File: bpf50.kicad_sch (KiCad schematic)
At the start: 39 parts

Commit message: 部品定数を入力　ただし未評価
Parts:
- C201, C230: value 10p -> NM
- C202, C229: value 10p -> 1000p
- C203, C205, C207, C209, C211, C213, C215, C217, C219, C221, C223, C225, C227: value 1p -> NM
- C204, C206, C210, C220, C226, C228: value 10p -> 150p
- C214, C218: value 10p -> 68p
- L203, L205: value 10n -> NM
- L204, L206: value 1u -> 33n
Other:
- note added: "2t D8.0mm L4.0mm"
- note added: "Butterworth 45M-57M 72p, 36p, 149p"
- company: (none) -> JK1MLY / PRUG
- title: (none) -> FM QRP TRCV

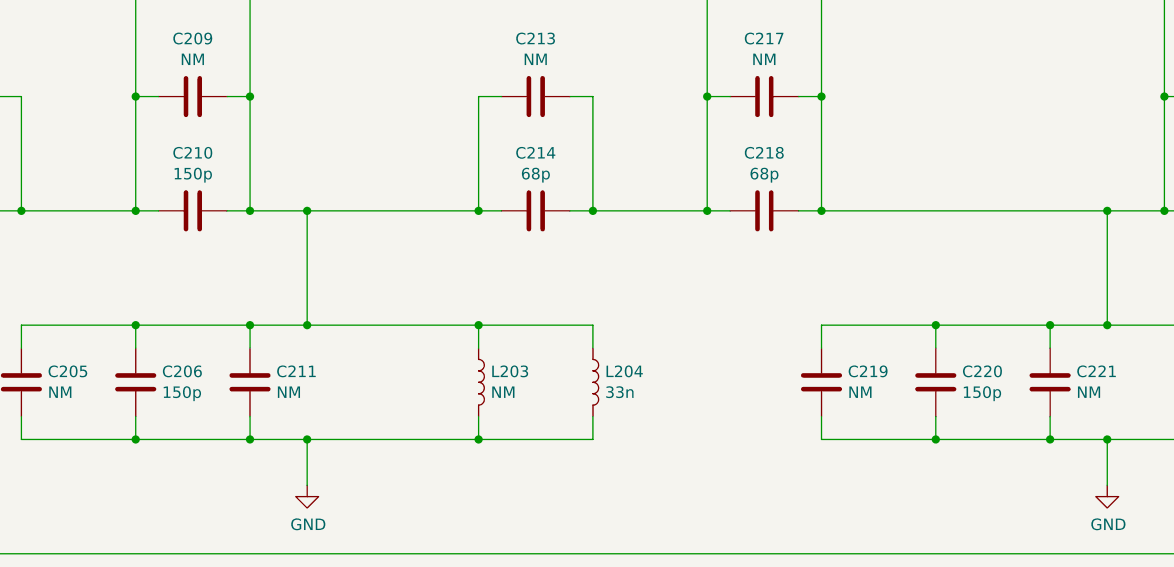
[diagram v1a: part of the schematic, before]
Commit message: バンドパスフィルタの定数を見直し（単体試験の反映）
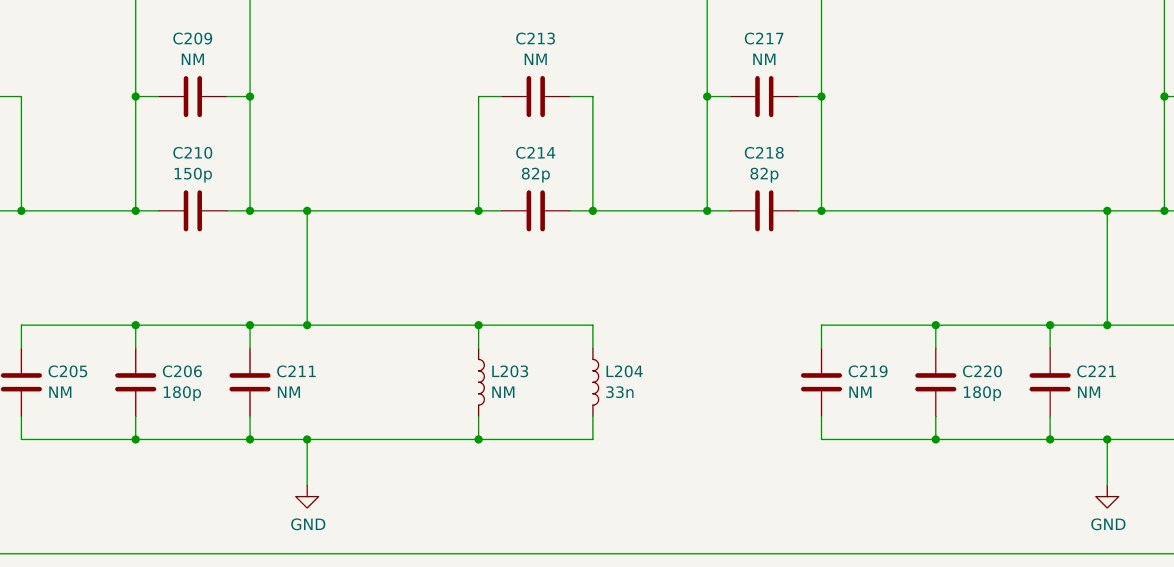
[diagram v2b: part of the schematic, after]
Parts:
- C206, C220: value 150p -> 180p
- C214, C218: value 68p -> 82p
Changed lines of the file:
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@@
       (effects (font (size 1.27 1.27)) (justify left))
     )
-    (property "Value" "150p" (id 1) (at 180.721 96.393 0)
+    (property "Value" "180p" (id 1) (at 180.721 96.393 0)
       (effects (font (size 1.27 1.27)) (justify left))
     )
@@
     (in_bom yes) (on_board yes)
     (property "Reference" "C218" (id 0) (at 158.75 69.7992 90))
-    (property "Value" "68p" (id 1) (at 158.75 72.1106 90))
+    (property "Value" "82p" (id 1) (at 158.75 72.1106 90))
     (property "Footprint" "Capacitor_THT:C_Disc_D3.4mm_W2.1mm_P2.50mm" (id 2) (at 162.56 75.2348 0)
       (effects (font (size 1.27 1.27)) hide)
@@
     (in_bom yes) (on_board yes)
     (property "Reference" "C214" (id 0) (at 133.35 69.7992 90))
-    (property "Value" "68p" (id 1) (at 133.35 72.1106 90))
+    (property "Value" "82p" (id 1) (at 133.35 72.1106 90))
     (property "Footprint" "Capacitor_THT:C_Disc_D3.4mm_W2.1mm_P2.50mm" (id 2) (at 137.16 75.2348 0)
       (effects (font (size 1.27 1.27)) hide)
@@
       (effects (font (size 1.27 1.27)) (justify left))
     )
-    (property "Value" "150p" (id 1) (at 91.821 96.393 0)
+    (property "Value" "180p" (id 1) (at 91.821 96.393 0)
       (effects (font (size 1.27 1.27)) (justify left))
     )

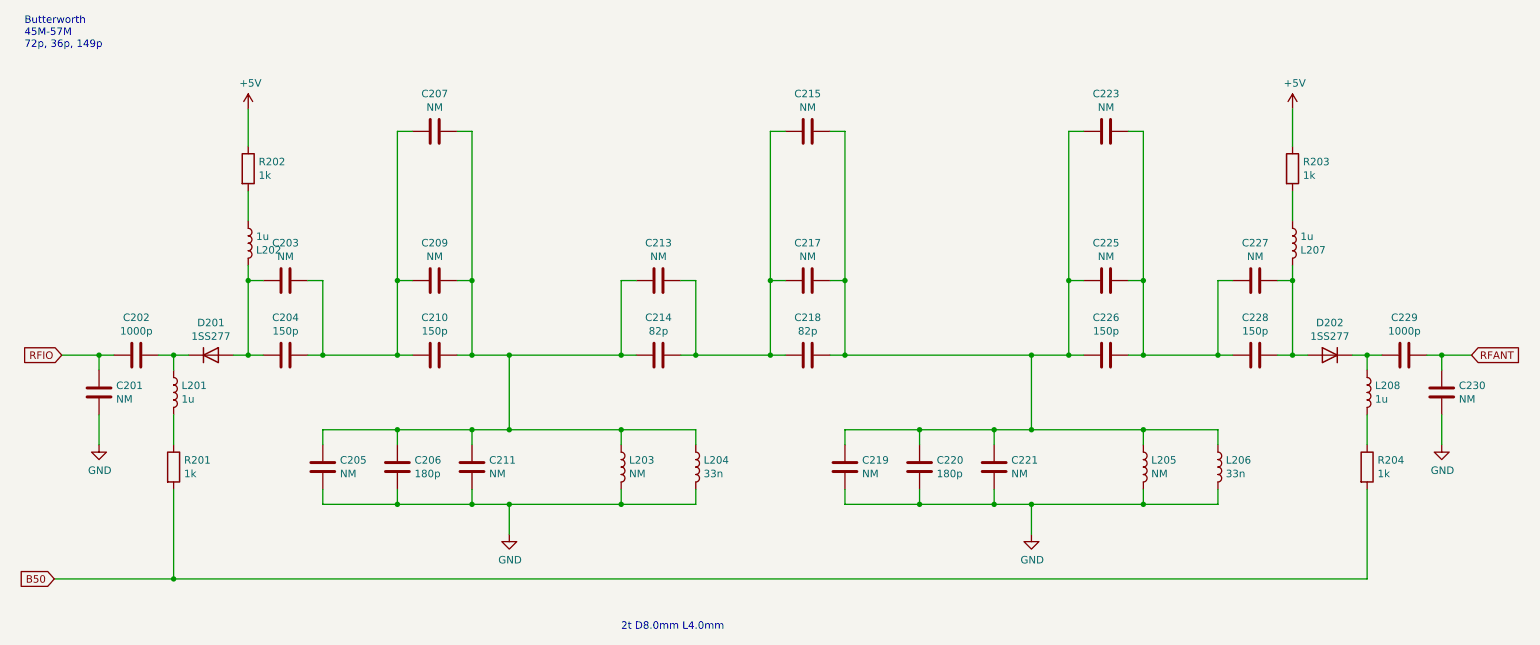
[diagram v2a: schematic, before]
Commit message: Add files via upload
フィルタ回路変更とジャンパクリーン
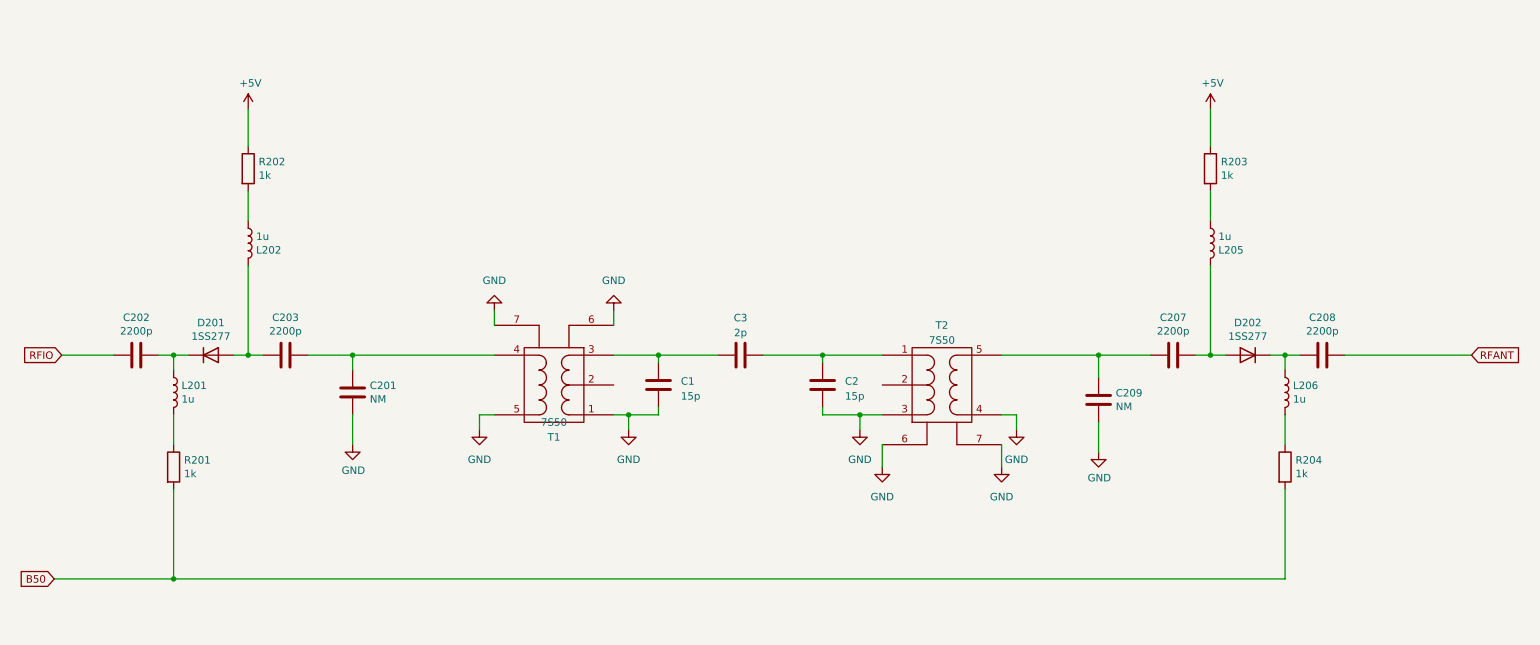
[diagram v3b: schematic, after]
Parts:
- removed C203, C205, C207, C209, C211, C213, C215, C217, C219, C221, C223, C225, C227: NM, digikey-footprints:0603, symbol Device:C
- removed C206, C220: 180p, Capacitor_THT:C_Disc_D3.4mm_W2.1mm_P2.50mm, symbol Device:C
- removed C210, C226: 150p, Capacitor_THT:C_Disc_D3.4mm_W2.1mm_P2.50mm, symbol Device:C
- removed C214, C218: 82p, Capacitor_THT:C_Disc_D3.4mm_W2.1mm_P2.50mm, symbol Device:C
- removed L203, L205: NM, Inductor_SMD:L_Murata_LQH2MCNxxxx02_2.0x1.6mm, symbol Device:L
- removed L204, L206: 33n, Resistor_THT:R_Axial_DIN0204_L3.6mm_D1.6mm_P5.08mm_Horizontal, symbol Device:L
- added C1, C2: 15p, Capacitor_THT:C_Disc_D3.0mm_W2.0mm_P2.50mm, symbol Device:C
- added C3: 2p, Capacitor_THT:C_Disc_D3.0mm_W2.0mm_P2.50mm, symbol Device:C
- added T1, T2: 7S50, usr-Library:coil_7mm, symbol Usr_Library:Transformer_SP_1S
- C202: value 1000p -> 2200p
- C203: renamed from C204; value 150p -> 2200p
- C207: renamed from C228; value 150p -> 2200p
- C208: renamed from C229; value 1000p -> 2200p
- renumbered C230 to C209, L207 to L205, L208 to L206
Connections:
- net GND: now also C1.2, C2.2, T1.1 (PR1), T1.5 (S2), T1.6 (G1), T1.7 (G2), T2.3 (PR2), T2.4 (S1), T2.6 (G1), T2.7 (G2)
- net RFANT: no longer C209.1
- net RFIO: no longer C201.1
- net at C203.2: now also C201.1, T1.4 (S1)
- net at C207.1: now also C209.1, T2.5 (S2)
- new net: C1.1, C3.2, T1.3 (PR2)
- new net: C2.1, C3.1, T2.1 (PR1)
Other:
- note removed: "2t D8.0mm L4.0mm"
- note removed: "Butterworth 45M-57M 72p, 36p, 149p"
- moved on the sheet: C201, C207, C208, C209, D202, L205, L206, R203, R204

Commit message: アップデート
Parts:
- added R102: 1k, Resistor_THT:R_Axial_DIN0207_L6.3mm_D2.5mm_P2.54mm_Vertical, symbol Device:R
- D201, D202: footprint Diode_THT:D_A-405_P2.54mm_Vertical_AnodeUp -> Diode_THT:D_T-1_P5.08mm_Horizontal
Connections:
- net +5V: now also R102.1
- net B50: now also R102.2
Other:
- note added: "47p 7.5T 33p 27p 33p 7.5T 47p"
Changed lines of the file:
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@@
   (junction (at 208.28 76.2) (diameter 0) (color 0 0 0 0)
   )
+  (junction (at 39.37 114.3) (diameter 0) (color 0 0 0 0)
+  )
   (junction (at 81.28 76.2) (diameter 0) (color 0 0 0 0)
   )
@@
     (stroke (width 0) (type default))
   )
+  (wire (pts (xy 39.37 114.3) (xy 50.8 114.3))
+    (stroke (width 0) (type default))
+  )
   (wire (pts (xy 240.03 76.2) (xy 240.03 78.74))
     (stroke (width 0) (type default))
@@
     (stroke (width 0) (type default))
   )
+  (wire (pts (xy 39.37 107.95) (xy 39.37 114.3))
+    (stroke (width 0) (type default))
+  )
   (wire (pts (xy 171.45 91.44) (xy 171.45 95.25))
     (stroke (width 0) (type default))
   )
-  (wire (pts (xy 30.48 114.3) (xy 50.8 114.3))
+  (wire (pts (xy 30.48 114.3) (xy 39.37 114.3))
     (stroke (width 0) (type default))
   )
@@
     (stroke (width 0) (type default))
   )
+  (wire (pts (xy 39.37 93.98) (xy 39.37 100.33))
+    (stroke (width 0) (type default))
+  )
   (wire (pts (xy 171.45 86.36) (xy 167.64 86.36))
     (stroke (width 0) (type default))
@@
   (wire (pts (xy 63.5 60.96) (xy 63.5 76.2))
     (stroke (width 0) (type default))
+  )
+  (text "47p 7.5T 33p 27p 33p 7.5T 47p" (at 113.03 43.18 0)
+    (effects (font (size 1.27 1.27)) (justify left bottom))
   )
   (global_label "RFIO" (shape input) (at 31.75 76.2 180) (fields_autoplaced)
@@
       (effects (font (size 1.27 1.27)))
     )
-    (property "Footprint" "Diode_THT:D_A-405_P2.54mm_Vertical_AnodeUp" (at 57.15 76.2 0)
+    (property "Footprint" "Diode_THT:D_T-1_P5.08mm_Horizontal" (at 57.15 76.2 0)
       (effects (font (size 1.27 1.27)) hide)
     )
@@
       (effects (font (size 1.27 1.27)))
     )
-    (property "Footprint" "Diode_THT:D_A-405_P2.54mm_Vertical_AnodeUp" (at 233.68 76.2 0)
+    (property "Footprint" "Diode_THT:D_T-1_P5.08mm_Horizontal" (at 233.68 76.2 0)
       (effects (font (size 1.27 1.27)) hide)
     )
@@
         )
       )
+    )
+  )
+  (symbol (lib_id "power:+5V") (at 39.37 93.98 0) (unit 1)
+    (in_bom yes) (on_board yes) (dnp no)
+    (property "Reference" "#PWR0102" (at 39.37 97.79 0)
+      (effects (font (size 1.27 1.27)) hide)
+    )
+    (property "Value" "+5V" (at 39.751 89.5858 0)
+      (effects (font (size 1.27 1.27)))
+    )
+    (property "Footprint" "" (at 39.37 93.98 0)
+      (effects (font (size 1.27 1.27)) hide)
+    )
+    (property "Datasheet" "" (at 39.37 93.98 0)
+      (effects (font (size 1.27 1.27)) hide)
+    )
+    (pin "1")
+    (instances
+      (project "fm_qrp2"
+        (path "/6d1d60ff-408a-47a7-892f-c5cf9ef6ca75/00000000-0000-0000-0000-000061d100f6"
+          (reference "#PWR0102") (unit 1)
+        )
+        (path "/6d1d60ff-408a-47a7-892f-c5cf9ef6ca75/00000000-0000-0000-0000-000061d104b7"
+          (reference "#PWR055") (unit 1)
+        )
+      )
+    )
+  )
+  (symbol (lib_id "Device:R") (at 39.37 104.14 0) (unit 1)
+    (in_bom yes) (on_board yes) (dnp no)
+    (property "Reference" "R102" (at 41.148 102.9716 0)
+      (effects (font (size 1.27 1.27)) (justify left))
+    )
+    (property "Value" "1k" (at 41.148 105.283 0)
+      (effects (font (size 1.27 1.27)) (justify left))
+    )
+    (property "Footprint" "Resistor_THT:R_Axial_DIN0207_L6.3mm_D2.5mm_P2.54mm_Vertical" (at 37.592 104.14 90)
+      (effects (font (size 1.27 1.27)) hide)
+    )
+    (property "Datasheet" "~" (at 39.37 104.14 0)
+      (effects (font (size 1.27 1.27)) hide)
+    )
+    (pin "1")
+    (pin "2")
+    (instances
+      (project "fm_qrp2"
+        (path "/6d1d60ff-408a-47a7-892f-c5cf9ef6ca75/00000000-0000-0000-0000-000061d100f6"
+          (reference "R102") (unit 1)
+        )
+        (path "/6d1d60ff-408a-47a7-892f-c5cf9ef6ca75/00000000-0000-0000-0000-000061d104b7"
+          (reference "R205") (unit 1)
+        )
+      )

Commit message: Add files via upload
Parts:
- C1, C2: value 15p -> 10p
- C202, C203, C207, C208: value 2200p -> 0.01u
- L201, L202, L205, L206: value 1u -> 10u
- R201, R202, R203, R204: value 1k -> 470
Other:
- note added: "L203,204はFCZ 7S50相当 サトー電気で入手可能"
- note removed: "47p 7.5T 33p 27p 33p 7.5T 47p"
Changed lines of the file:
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@@
   (title_block
     (title "FM QRP TRCV")
-    (date "2022-03-12")
+    (date "2023-08-12")
     (rev "1")
     (company "JK1MLY / PRUG")
@@
     (stroke (width 0) (type default))
   )
-  (text "47p 7.5T 33p 27p 33p 7.5T 47p" (at 113.03 43.18 0)
+  (text "L203,204はFCZ 7S50相当\nサトー電気で入手可能" (at 113.03 43.18 0)
     (effects (font (size 1.27 1.27)) (justify left bottom))
   )
@@
       (effects (font (size 1.27 1.27)) (justify left))
     )
-    (property "Value" "1u" (at 241.3762 83.693 0)
+    (property "Value" "10u" (at 241.3762 83.693 0)
       (effects (font (size 1.27 1.27)) (justify left))
     )
@@
       (effects (font (size 1.27 1.27)) (justify left))
     )
-    (property "Value" "1k" (at 65.278 45.593 0)
+    (property "Value" "470" (at 65.278 45.593 0)
       (effects (font (size 1.27 1.27)) (justify left))
     )
@@
       (effects (font (size 1.27 1.27)) hide)
     )
-    (property "Datasheet" "~" (at 63.5 44.45 0)
+    (property "Datasheet" "R-25471" (at 63.5 44.45 0)
       (effects (font (size 1.27 1.27)) hide)
     )
@@
       (effects (font (size 1.27 1.27)) (justify left))
     )
-    (property "Value" "1k" (at 241.808 96.393 0)
+    (property "Value" "470" (at 241.808 96.393 0)
       (effects (font (size 1.27 1.27)) (justify left))
     )
@@
       (effects (font (size 1.27 1.27)) hide)
     )
-    (property "Datasheet" "~" (at 240.03 95.25 0)
+    (property "Datasheet" "R-25471" (at 240.03 95.25 0)
       (effects (font (size 1.27 1.27)) hide)
     )
@@
       (effects (font (size 1.27 1.27)))
     )
-    (property "Value" "2200p" (at 69.85 72.1106 90)
+    (property "Value" "0.01u" (at 69.85 72.1106 90)
       (effects (font (size 1.27 1.27)))
     )
@@
       (effects (font (size 1.27 1.27)) hide)
     )
-    (property "Datasheet" "~" (at 69.85 76.2 0)
+    (property "Datasheet" "sato" (at 69.85 76.2 0)
       (effects (font (size 1.27 1.27)) hide)
     )
@@
       (effects (font (size 1.27 1.27)))
     )
-    (property "Value" "2200p" (at 220.98 72.1106 90)
+    (property "Value" "0.01u" (at 220.98 72.1106 90)
       (effects (font (size 1.27 1.27)))
     )
@@
       (effects (font (size 1.27 1.27)) hide)
     )
-    (property "Datasheet" "~" (at 220.98 76.2 0)
+    (property "Datasheet" "sato" (at 220.98 76.2 0)
       (effects (font (size 1.27 1.27)) hide)
     )
@@
       (effects (font (size 1.27 1.27)) (justify left))
     )
-    (property "Value" "1u" (at 52.1462 83.693 0)
+    (property "Value" "10u" (at 52.1462 83.693 0)
       (effects (font (size 1.27 1.27)) (justify left))
     )
@@
       (effects (font (size 1.27 1.27)) (justify left))
     )
-    (property "Value" "1k" (at 52.578 96.393 0)
+    (property "Value" "470" (at 52.578 96.393 0)
       (effects (font (size 1.27 1.27)) (justify left))
     )
@@
       (effects (font (size 1.27 1.27)) hide)
     )
-    (property "Datasheet" "~" (at 50.8 95.25 0)
+    (property "Datasheet" "R-25471" (at 50.8 95.25 0)
       (effects (font (size 1.27 1.27)) hide)
     )
@@
       (effects (font (size 1.27 1.27)) (justify left))
     )
-    (property "Value" "1u" (at 64.8462 56.007 0)
+    (property "Value" "10u" (at 64.8462 56.007 0)
       (effects (font (size 1.27 1.27)) (justify left))
     )
@@
       (effects (font (size 1.27 1.27)) (justify left))
     )
-    (property "Value" "1k" (at 229.108 45.593 0)
+    (property "Value" "470" (at 229.108 45.593 0)
       (effects (font (size 1.27 1.27)) (justify left))
     )
@@
       (effects (font (size 1.27 1.27)) hide)
     )
-    (property "Datasheet" "~" (at 227.33 44.45 0)
+    (property "Datasheet" "R-25471" (at 227.33 44.45 0)
       (effects (font (size 1.27 1.27)) hide)
     )
@@
       (effects (font (size 1.27 1.27)) (justify left))
     )
-    (property "Value" "1u" (at 228.6762 56.007 0)
+    (property "Value" "10u" (at 228.6762 56.007 0)
       (effects (font (size 1.27 1.27)) (justify left))
     )
@@
       (effects (font (size 1.27 1.27)))
     )
-    (property "Value" "2200p" (at 246.38 72.1106 90)
+    (property "Value" "0.01u" (at 246.38 72.1106 90)
       (effects (font (size 1.27 1.27)))
     )
@@
       (effects (font (size 1.27 1.27)) hide)
     )
-    (property "Datasheet" "~" (at 246.38 76.2 0)
+    (property "Datasheet" "sato" (at 246.38 76.2 0)
       (effects (font (size 1.27 1.27)) hide)
     )
@@
       (effects (font (size 1.27 1.27)))
     )
-    (property "Value" "2200p" (at 44.45 72.1106 90)
+    (property "Value" "0.01u" (at 44.45 72.1106 90)
       (effects (font (size 1.27 1.27)))
     )
@@
       (effects (font (size 1.27 1.27)) hide)
     )
-    (property "Datasheet" "~" (at 44.45 76.2 0)
+    (property "Datasheet" "sato" (at 44.45 76.2 0)
       (effects (font (size 1.27 1.27)) hide)
     )
@@
       (effects (font (size 1.27 1.27)))
     )
-    (property "Value" "7S50" (at 115.5573 87.63 0)
+    (property "Value" "7S50" (at 115.57 92.71 0)
       (effects (font (size 1.27 1.27)))
     )
@@
       (effects (font (size 1.27 1.27)) hide)
     )
-    (property "Datasheet" "~" (at 115.57 81.28 0)
+    (property "Datasheet" "sato" (at 115.57 81.28 0)
       (effects (font (size 1.27 1.27)) hide)
     )
@@
       (effects (font (size 1.27 1.27)) hide)
     )
-    (property "Datasheet" "~" (at 181.61 81.28 0)
+    (property "Datasheet" "sato" (at 181.61 81.28 0)
       (effects (font (size 1.27 1.27)) hide)
     )
@@
       (effects (font (size 1.27 1.27)) (justify left))
     )
-    (property "Value" "15p" (at 165.1 83.185 0)
+    (property "Value" "10p" (at 165.1 83.185 0)
       (effects (font (size 1.27 1.27)) (justify left))
     )
@@
       (effects (font (size 1.27 1.27)) hide)
     )
-    (property "Datasheet" "~" (at 161.29 81.28 0)
+    (property "Datasheet" "sato" (at 161.29 81.28 0)
       (effects (font (size 1.27 1.27)) hide)
     )
@@
       (effects (font (size 1.27 1.27)) hide)
     )
-    (property "Datasheet" "~" (at 147.32 76.2 0)
+    (property "Datasheet" "sato" (at 147.32 76.2 0)
       (effects (font (size 1.27 1.27)) hide)
     )
@@
       (effects (font (size 1.27 1.27)) hide)
     )
-    (property "Datasheet" "~" (at 39.37 104.14 0)
+    (property "Datasheet" "R-25102" (at 39.37 104.14 0)
       (effects (font (size 1.27 1.27)) hide)
     )
@@
       (effects (font (size 1.27 1.27)) (justify left))
     )
-    (property "Value" "15p" (at 137.16 83.185 0)
+    (property "Value" "10p" (at 137.16 83.185 0)
       (effects (font (size 1.27 1.27)) (justify left))
     )
@@
       (effects (font (size 1.27 1.27)) hide)
     )
-    (property "Datasheet" "~" (at 133.35 81.28 0)
-      (effects (font (size 1.27 1.27)) hide)
-    )
+    (property "Datasheet" "sato" (at 133.35 81.28 0)
+      (effects (font (size 1.27 1.27)) hide)
+    )
